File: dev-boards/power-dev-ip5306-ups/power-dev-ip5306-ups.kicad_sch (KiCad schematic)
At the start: 26 parts, among them J1 USB_C_Receptacle_PowerOnly_6P, J2 USB_C_Receptacle_PowerOnly_6P, Q1 AO3401A, Q2 AO3401A, SW1 SW_SPDT, U1 IP5306, U2 XB5350D0, U3 MT3608

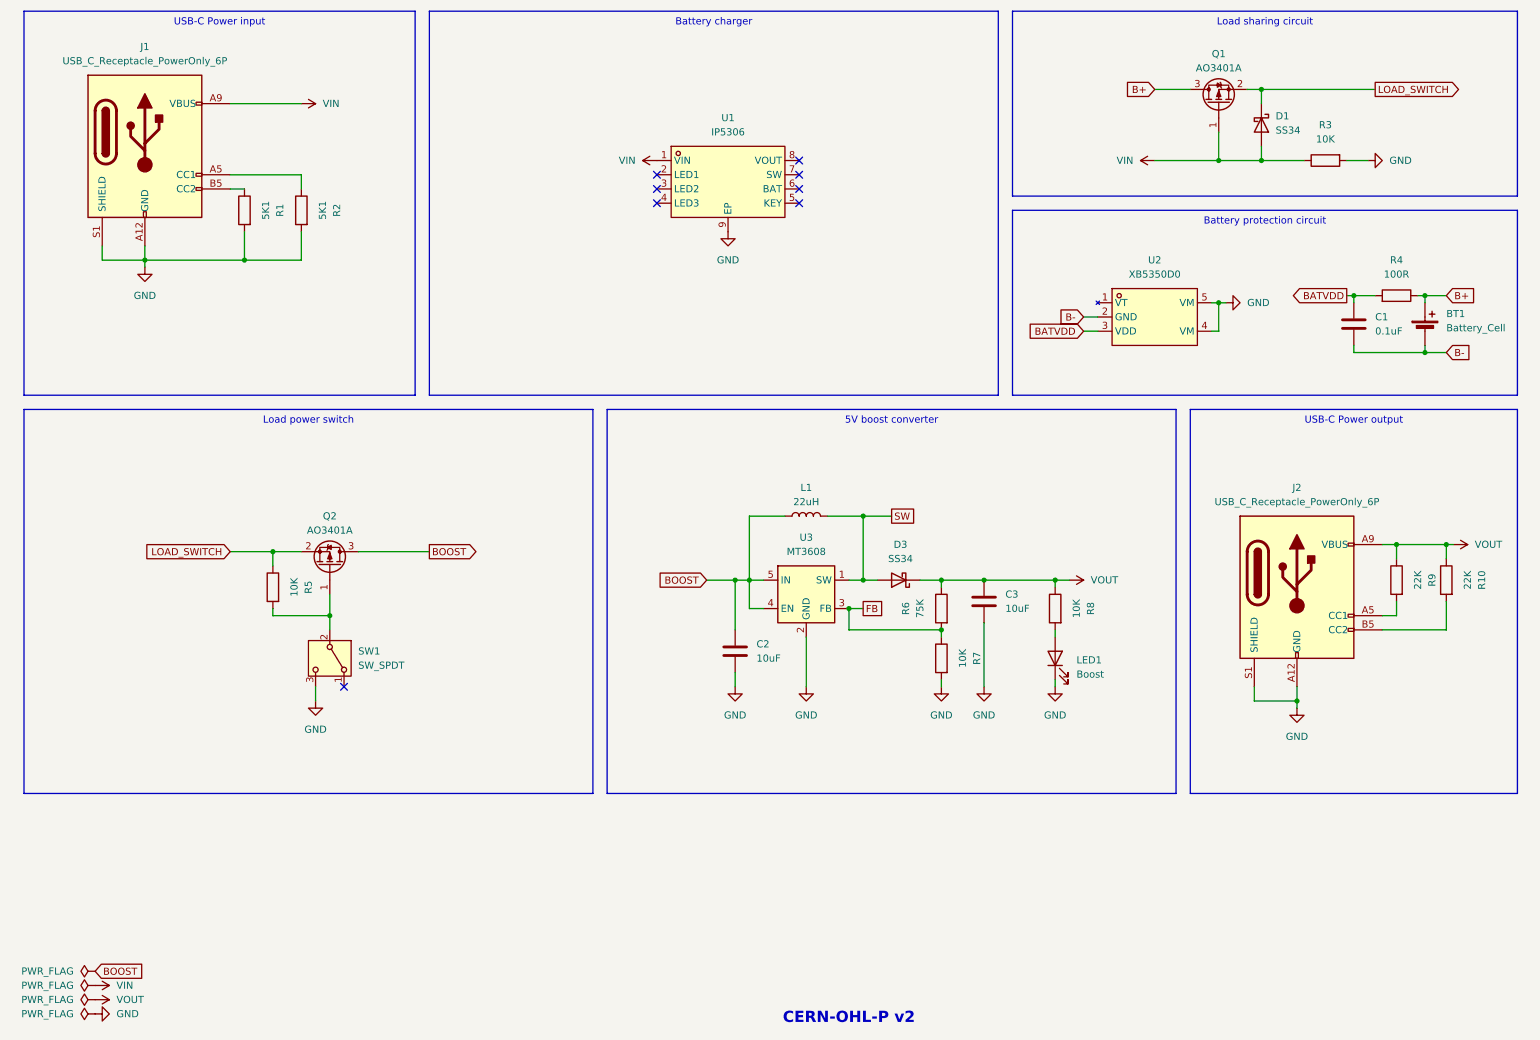
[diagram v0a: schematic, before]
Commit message: Split schematic into hierarchical sheets
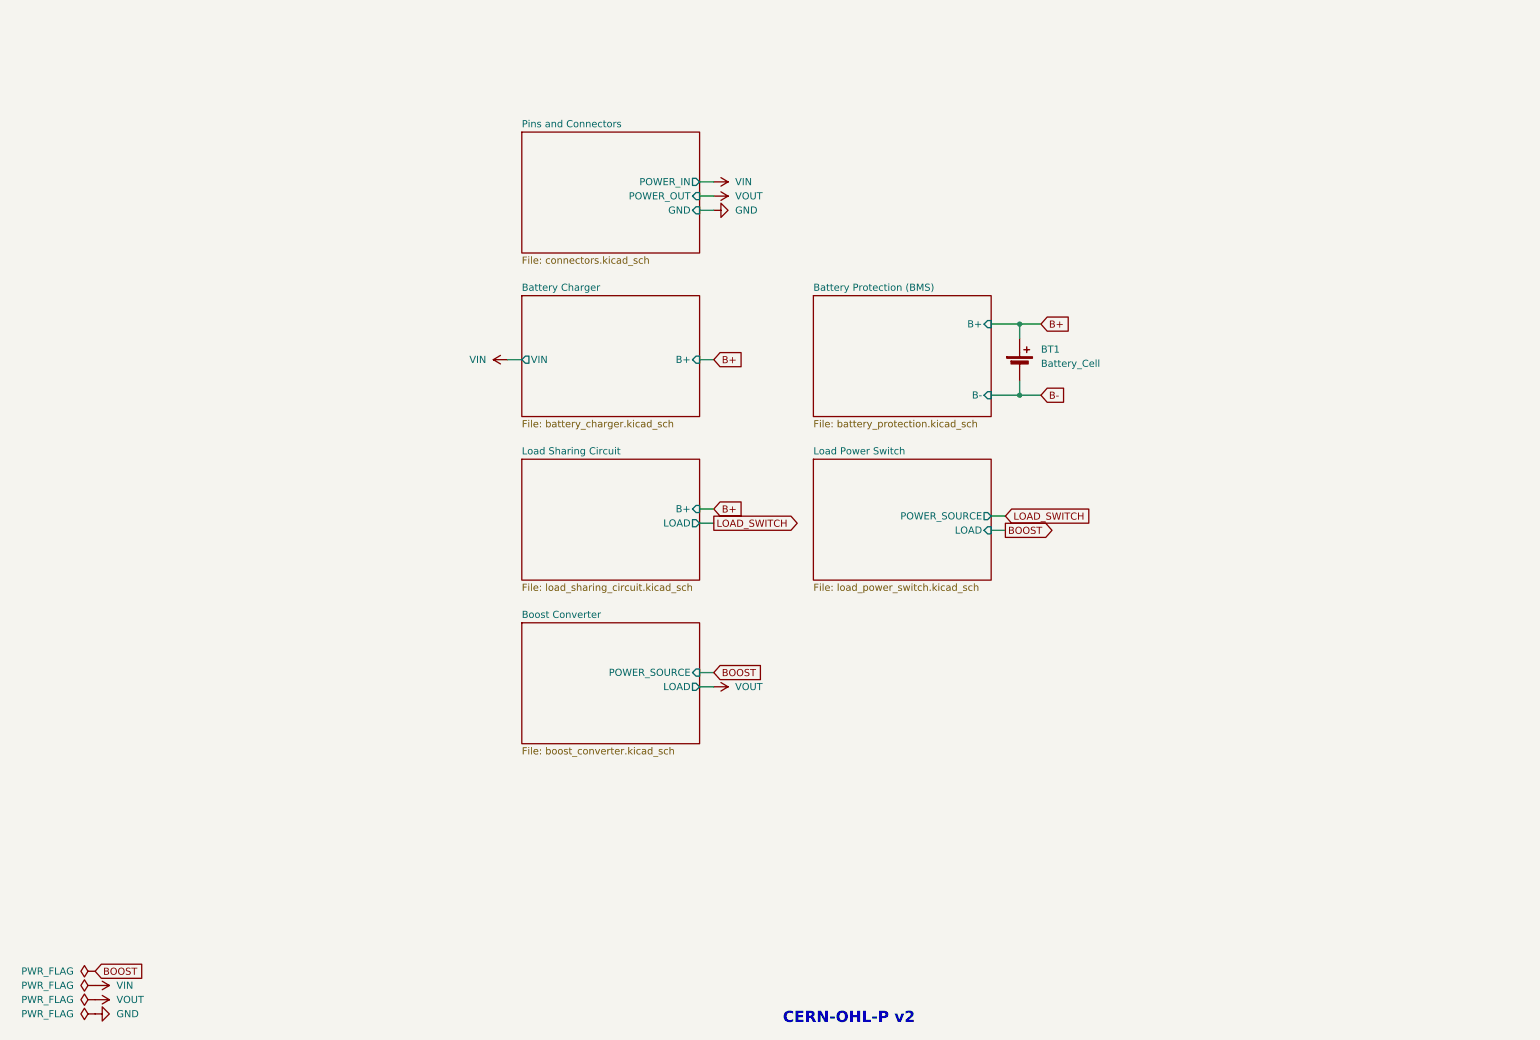
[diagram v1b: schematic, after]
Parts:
- removed C1: 0.1uF, Capacitor_SMD:C_0402_1005Metric, symbol Device:C
- removed C2: 10uF, Capacitor_SMD:C_0603_1608Metric, symbol Device:C
- removed C3: 10uF, Capacitor_SMD:C_0402_1005Metric, symbol Device:C
- removed D1, D3: SS34, custom:D_SMA_simple, symbol Diode:SS34
- removed J1, J2: USB_C_Receptacle_PowerOnly_6P, custom:USB_C_Receptacle_GCT_USB4125-xx-x_6P_TopMnt_Horizontal_handsolder, symbol Connector:USB_C_Receptacle_PowerOnly_6P
- removed L1: 22uH, lcsc:IND-SMD_L7.0-W6.6, symbol Device:L
- removed LED1: Boost, custom:LED_0805_2012Metric_Pad1.15x1.40mm_HandSolder_simple, symbol Device:LED
- removed Q1, Q2: AO3401A, Package_TO_SOT_SMD:SOT-23, symbol Transistor_FET:AO3401A
- removed R1, R2: 5K1, Resistor_SMD:R_0402_1005Metric, symbol Device:R
- removed R10, R9: 22K, Resistor_SMD:R_0402_1005Metric, symbol Device:R
- removed R3, R5, R7, R8: 10K, Resistor_SMD:R_0402_1005Metric, symbol Device:R
- removed R4: 100R, Resistor_SMD:R_0805_2012Metric_Pad1.20x1.40mm_HandSolder, symbol Device:R
- removed R6: 75K, Resistor_SMD:R_0402_1005Metric, symbol Device:R
- removed SW1: SW_SPDT, custom:SW-TH_DEALON_SS-12D01-GX_simple, symbol Switch:SW_SPDT
- removed U1: IP5306, custom:SOIC-8-1EP_3.9x4.9mm_P1.27mm_EP2.41x3.3mm_ThermalVias_CustomVias_Large, symbol lcsc:IP5306
- removed U2: XB5350D0, custom:SOT-23-5_simple, symbol lcsc:XB5350D0
- removed U3: MT3608, Package_TO_SOT_SMD:SOT-23-6, symbol lcsc:MT3608
- BT1: footprint custom:JST_XH_B2B-XH-A_1x02_P2.50mm_Vertical_simple_pad2gnd -> lcsc:BAT-TH_18650-A5BJ001
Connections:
- no-connect marks 8 -> 0
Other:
- added sheet Battery Charger (battery_charger.kicad_sch)
- added sheet Battery Protection (BMS) (battery_protection.kicad_sch)
- added sheet Boost Converter (boost_converter.kicad_sch)
- added sheet Load Power Switch (load_power_switch.kicad_sch)
- added sheet Load Sharing Circuit (load_sharing_circuit.kicad_sch)
- added sheet Pins and Connectors (connectors.kicad_sch)

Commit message: Add battery sense pins, more connectors
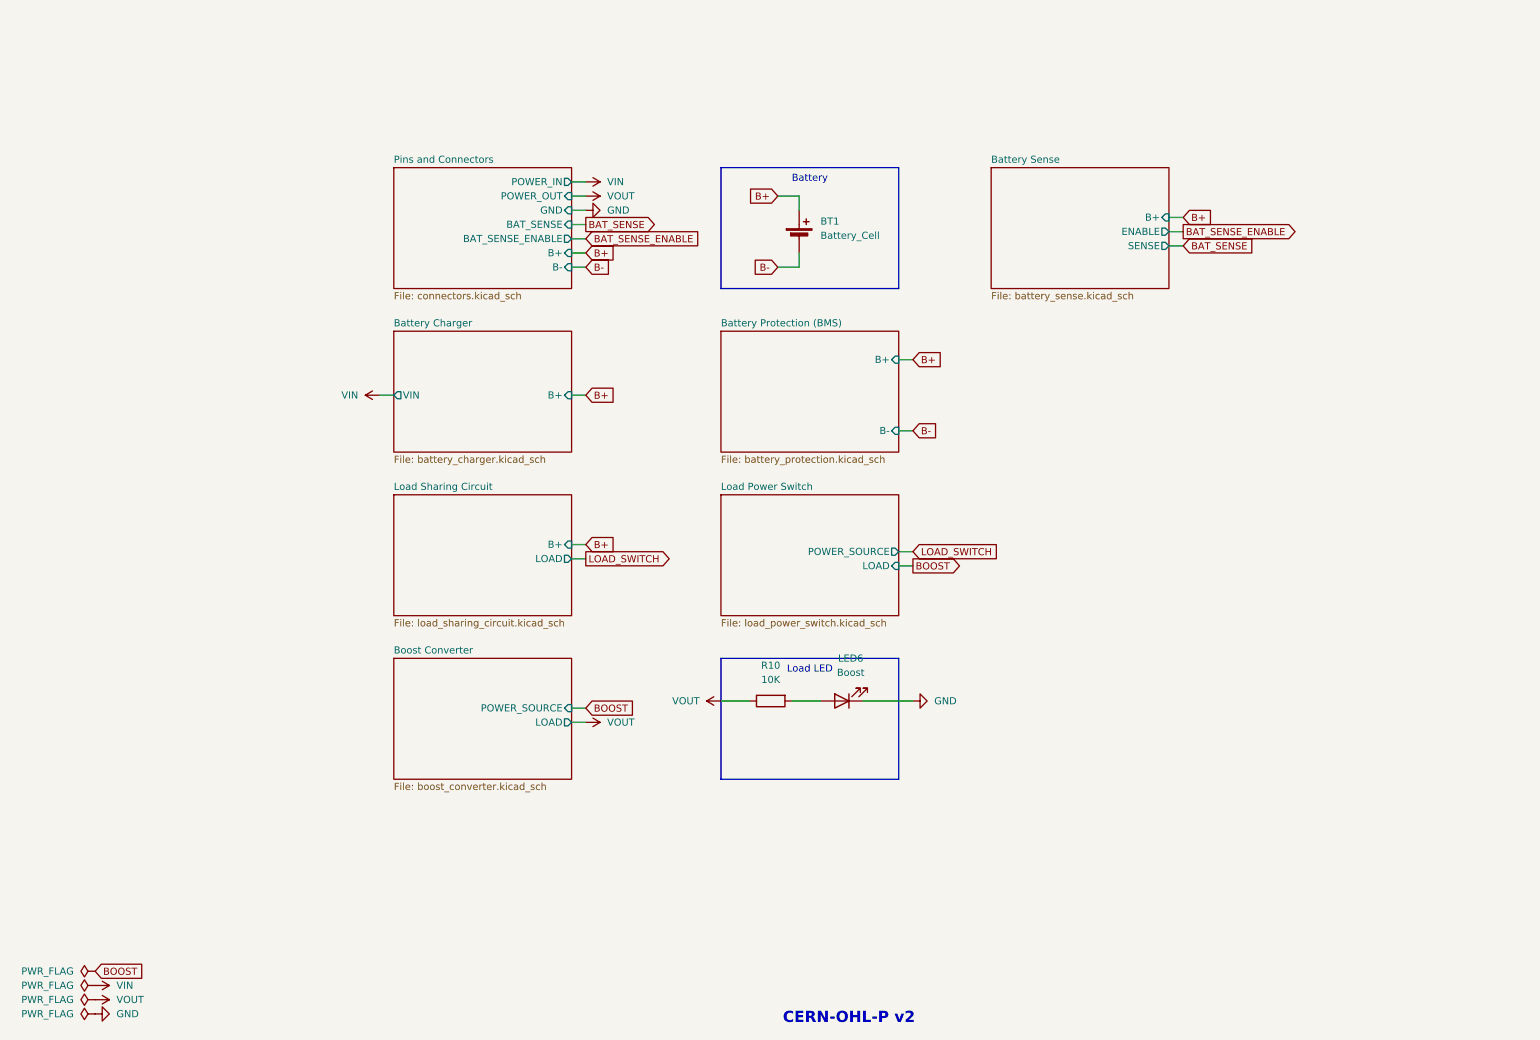
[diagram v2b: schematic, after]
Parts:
- added LED6: Boost, custom:LED_0805_2012Metric_Pad1.15x1.40mm_HandSolder_simple, symbol Device:LED
- added R10: 10K, Resistor_SMD:R_0402_1005Metric, symbol Device:R
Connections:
- net GND: now also LED6.1 (K)
- net VOUT: now also R10.1
- new net: LED6.2 (A), R10.2
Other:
- added sheet Battery Sense (battery_sense.kicad_sch)
- sheet Pins and Connectors ports: added B+, B-, BAT_SENSE, BAT_SENSE_ENABLE; removed none

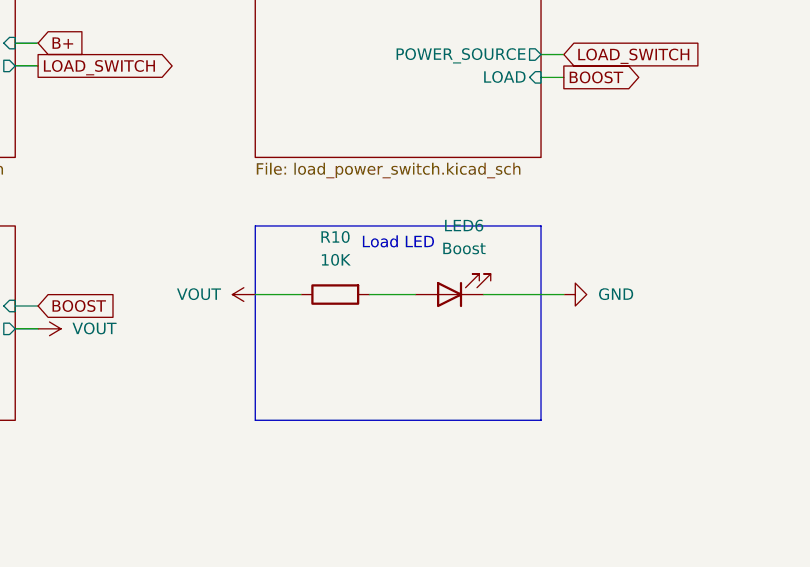
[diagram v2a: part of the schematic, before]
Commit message: Design power-dev-ip5306-ups PCB
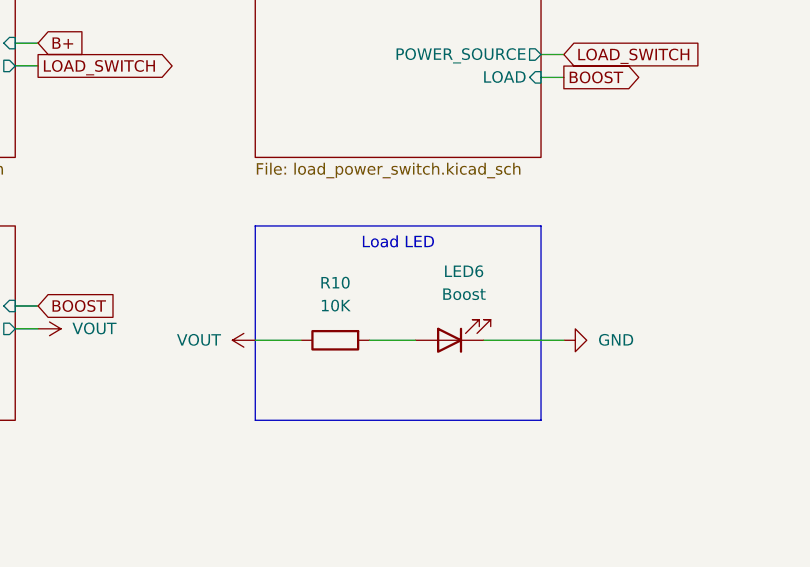
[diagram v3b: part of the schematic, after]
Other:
- moved on the sheet: LED6, R10
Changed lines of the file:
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@@
 	(wire
 		(pts
-			(xy 139.7 138.43) (xy 144.78 138.43)
-		)
-		(stroke
-			(width 0)
-			(type default)
-		)
-	)
-	(wire
-		(pts
-			(xy 152.4 138.43) (xy 157.48 138.43)
+			(xy 139.7 143.51) (xy 144.78 143.51)
+		)
+		(stroke
+			(width 0)
+			(type default)
+		)
+	)
+	(wire
+		(pts
+			(xy 152.4 143.51) (xy 157.48 143.51)
 		)
 		(stroke
@@
 	(wire
 		(pts
-			(xy 173.99 138.43) (xy 165.1 138.43)
+			(xy 173.99 143.51) (xy 165.1 143.51)
 		)
 		(stroke
@@
 	(symbol
 		(lib_id "Device:R")
-		(at 148.59 138.43 90)
+		(at 148.59 143.51 90)
 		(mirror x)
 		(unit 1)
@@
 		(dnp no)
 		(property "Reference" "R10"
-			(at 148.59 132.08 90)
+			(at 148.59 137.16 90)
 			(effects
 				(font
@@
 		)
 		(property "Value" "10K"
-			(at 148.59 134.62 90)
+			(at 148.59 139.7 90)
 			(effects
 				(font
@@
 		)
 		(property "Footprint" "Resistor_SMD:R_0402_1005Metric"
-			(at 148.59 136.652 90)
+			(at 148.59 141.732 90)
 			(effects
 				(font
@@
 		)
 		(property "Datasheet" "~"
-			(at 148.59 138.43 0)
+			(at 148.59 143.51 0)
 			(effects
 				(font
@@
 		)
 		(property "Description" "Resistor"
-			(at 148.59 138.43 0)
+			(at 148.59 143.51 0)
 			(effects
 				(font
@@
 		)
 		(property "LCSC Part" "C25744"
-			(at 148.59 138.43 0)
+			(at 148.59 143.51 0)
 			(effects
 				(font
@@
 	(symbol
 		(lib_id "power:+5V")
-		(at 139.7 138.43 90)
+		(at 139.7 143.51 90)
 		(unit 1)
 		(exclude_from_sim no)
@@
 		(fields_autoplaced yes)
 		(property "Reference" "#PWR017"
-			(at 143.51 138.43 0)
+			(at 143.51 143.51 0)
 			(effects
 				(font
@@
 		)
 		(property "Value" "VOUT"
-			(at 135.89 138.4299 90)
+			(at 135.89 143.5099 90)
 			(effects
 				(font
@@
 		)
 		(property "Footprint" ""
-			(at 139.7 138.43 0)
+			(at 139.7 143.51 0)
 			(effects
 				(font
@@
 		)
 		(property "Datasheet" ""
-			(at 139.7 138.43 0)
+			(at 139.7 143.51 0)
 			(effects
 				(font
@@
 		)
 		(property "Description" "Power symbol creates a global label with name \"+5V\""
-			(at 139.7 138.43 0)
+			(at 139.7 143.51 0)
 			(effects
 				(font
@@
 	(symbol
 		(lib_id "power:GND")
-		(at 173.99 138.43 90)
+		(at 173.99 143.51 90)
 		(unit 1)
 		(exclude_from_sim no)
@@
 		(fields_autoplaced yes)
 		(property "Reference" "#PWR012"
-			(at 180.34 138.43 0)
+			(at 180.34 143.51 0)
 			(effects
 				(font
@@
 		)
 		(property "Value" "GND"
-			(at 177.8 138.4299 90)
+			(at 177.8 143.5099 90)
 			(effects
 				(font
@@
 		)
 		(property "Footprint" ""
-			(at 173.99 138.43 0)
+			(at 173.99 143.51 0)
 			(effects
 				(font
@@
 		)
 		(property "Datasheet" ""
-			(at 173.99 138.43 0)
+			(at 173.99 143.51 0)
 			(effects
 				(font
@@
 		)
 		(property "Description" "Power symbol creates a global label with name \"GND\" , ground"
-			(at 173.99 138.43 0)
+			(at 173.99 143.51 0)
 			(effects
 				(font
@@
 	(symbol
 		(lib_id "Device:LED")
-		(at 161.29 138.43 180)
+		(at 161.29 143.51 180)
 		(unit 1)
 		(exclude_from_sim no)
@@
 		(fields_autoplaced yes)
 		(property "Reference" "LED6"
-			(at 162.8775 130.81 0)
+			(at 162.8775 135.89 0)
 			(effects
 				(font
@@
 		)
 		(property "Value" "Boost"
-			(at 162.8775 133.35 0)
+			(at 162.8775 138.43 0)
 			(effects
 				(font
@@
 		)
 		(property "Footprint" "custom:LED_0805_2012Metric_Pad1.15x1.40mm_HandSolder_simple"
-			(at 161.29 138.43 0)
+			(at 161.29 143.51 0)
 			(effects
 				(font
@@
 		)
 		(property "Datasheet" "~"
-			(at 161.29 138.43 0)
+			(at 161.29 143.51 0)
 			(effects
 				(font
@@
 		)
 		(property "Description" "Light emitting diode"
-			(at 161.29 138.43 0)
+			(at 161.29 143.51 0)
 			(effects
 				(font
@@
 		)
 		(property "LCSC Part" ""
-			(at 161.29 138.43 0)
-			(effects
-				(font
+			(at 161.29 143.51 0)
+			(effects
+				(font
